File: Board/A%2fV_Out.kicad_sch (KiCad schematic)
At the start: 12 parts, among them J1 HDMI_A

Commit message: work on hdmi
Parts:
- removed SCL1, SDA1, SH1: Conn_01x01_Pin, Connector_PinHeader_1.00mm:PinHeader_1x01_P1.00mm_Vertical, symbol Connector:Conn_01x01_Pin
- added C23, C33: 47u, Capacitor_SMD:C_0805_2012Metric_Pad1.18x1.45mm_HandSolder, symbol Device:C_Polarized
- added C50, C51: 0.1u, csa_ultracpu:C0603, symbol csa_ultracpu-eagle-import:C-EUC0603
- added JP16, JP17, JP18: SolderJumper_2_Open, Jumper:SolderJumper-2_P1.3mm_Open_RoundedPad1.0x1.5mm, symbol Jumper:SolderJumper_2_Open
- added R13, R14, R7, R8: 1k, Resistor_SMD:R_0603_1608Metric_Pad0.98x0.95mm_HandSolder, symbol Device:R
- added U3: ~, Package_DFN_QFN:Diodes_ZL32_TQFN-32-1EP_3x6mm_P0.4mm_EP1.25x3.5mm, symbol HDMI:PI3HDX511Z
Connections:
- net GND: now also J1.SH, C23.2, C33.2, C50.2, C51.2, R14.1, R8.1, U3.14 (GND), U3.31 (GND), U3.32 (GND)
- net HDMI-CK+: now also U3.9 (RCK_N); no longer J1.10 (CK+)
- net HDMI-CK-: now also U3.10 (RCK_P); no longer J1.12 (CK-)
- net HDMI-D0+: now also U3.7 (RD0_N); no longer J1.7 (D0+)
- net HDMI-D0-: now also U3.8 (RD0_P); no longer J1.9 (D0-)
- net HDMI-D1+: now also U3.5 (RD1_N); no longer J1.4 (D1+)
- net HDMI-D1-: now also U3.6 (RD1_P); no longer J1.6 (D1-)
- net HDMI-D2+: now also U3.3 (RD2_N); no longer J1.1 (D2+)
- net HDMI-D2-: now also U3.4 (RD2_P); no longer J1.3 (D2-)
- net at J1.15 (SCL): now also U3.27 (SCL_SINK)
- net at HPD1.1 (Pin_1): now also U3.11 (HPD_SRC); no longer J1.19 (HPD)
- net at J1.16 (SDA): now also U3.28 (SDA_SINK)
- new net: JP17.1 (A), R8.2
- new net: JP17.2 (B), U3.16 (OC_S0)
- new net: R14.2, U3.15 (TEST)
- new net: JP16.1 (A), R13.2
- new net: JP16.2 (B), U3.30 (/OE)
- new net: C23.1, U3.2 (CEXT)
- new net: JP18.2 (B), U3.17 (EQ_S0)
- new net: J1.12 (CK-), U3.18 (TCK_P)
- new net: J1.10 (CK+), U3.19 (TCK_N)
- new net: J1.9 (D0-), U3.20 (TD0_P)
- new net: J1.7 (D0+), U3.21 (TD0_N)
- new net: J1.6 (D1-), U3.23 (TD1_P)
- new net: J1.4 (D1+), U3.24 (TD1_N)
- new net: J1.3 (D2-), U3.25 (TD2_P)
- new net: J1.1 (D2+), U3.26 (TD2_N)
- new net: J1.19 (HPD), U3.29 (HPD_SINK)
- new net: JP18.1 (A), R7.2
- new net I2C_SCL: U3.13 (SCL_SRC)
- new net I2C_SDA: U3.12 (SDA_SRC)
- new net V33: C33.1, C50.1, C51.1, R13.1, R7.1, U3.1 (VCC), U3.22 (VCC)
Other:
- note added: "Note: PI3HDX511D datasheet has reference schematics that also swap signal polarities (on differential signals)"
- note added: "V1.0B: - Added "Brown Fix" V1.1A: - 3.3/5V level converter - VGA ESD protection diodes V1.4A: - go from RGBI to 6bit RGB (2b/col) (replacing IC6 "brownfix" in the process V2.2A: - go from VGA to HDMI - add HDMI re-driver IC"
- note removed: "V1.0B: - Added "Brown Fix" V1.1A: - 3.3/5V level converter - VGA ESD protection diodes V1.4A: - go from RGBI to 6bit RGB (2b/col) (replacing IC6 "brownfix" in the process V2.2A: - go from VGA to HDMI"
- moved on the sheet: CEC1, CKS1, D0S1, D1S1, D2S1, HPD1, J1, JP14, UTIL1

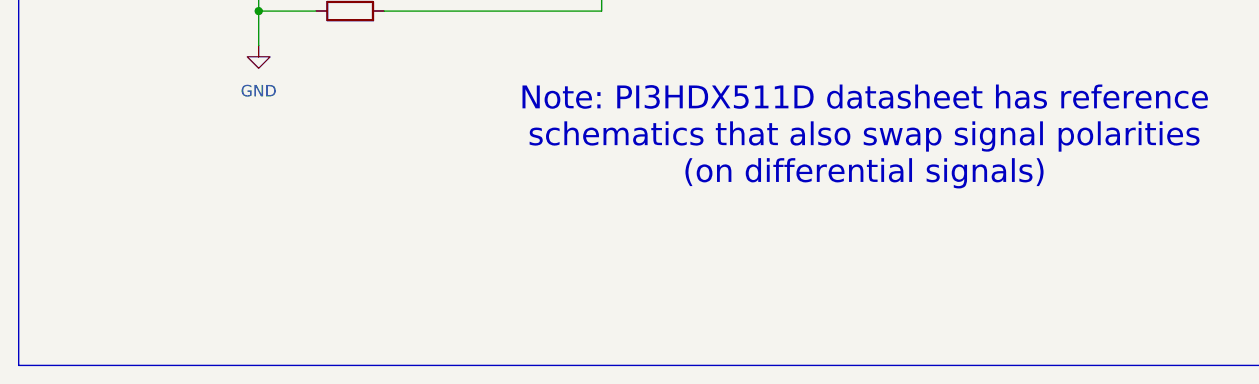
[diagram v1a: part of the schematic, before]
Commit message: start working on 3.0 with larger FPGA
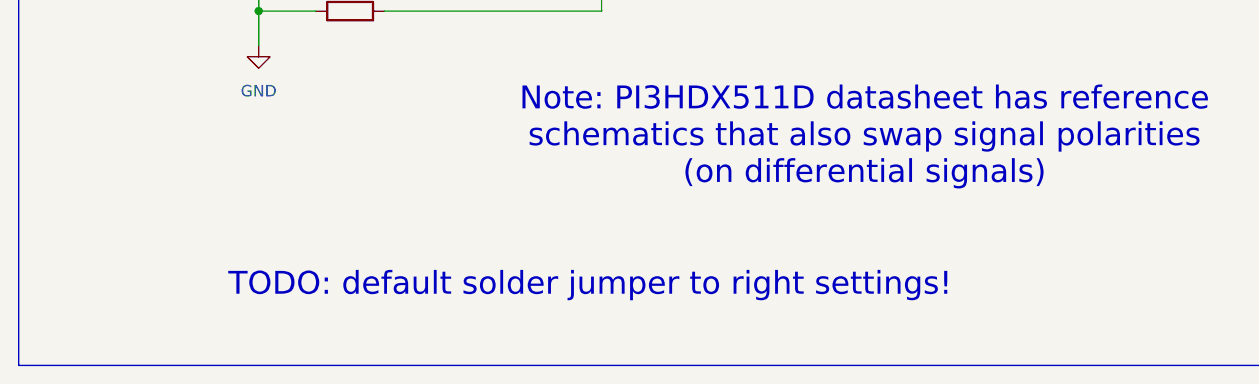
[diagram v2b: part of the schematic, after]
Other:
- note added: "TODO: default solder jumper to right settings!"
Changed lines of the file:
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@@
+		)
+	)
+	(text "TODO: default solder jumper to right settings!\n"
+		(exclude_from_sim no)
+		(at 71.12 166.37 0)
+		(effects
+			(font
+				(size 2.54 2.54)
+			)
 		)
 	)

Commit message: layout work
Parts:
- added C52, C53, C59, C60, C61, C62, C63, C72: 100n, Capacitor_SMD:C_0603_1608Metric_Pad1.08x0.95mm_HandSolder, symbol csa_ultracpu-eagle-import:C-EUC0603
- C50, C51: value 0.1u -> 100n; footprint csa_ultracpu:C0603 -> Capacitor_SMD:C_0603_1608Metric_Pad1.08x0.95mm_HandSolder
- U3: value ~ -> (none)
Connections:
- net HDMI-CK+: now also C62.1; no longer U3.9 (RCK_N)
- net HDMI-CK-: now also C72.1; no longer U3.10 (RCK_P)
- net HDMI-D0+: now also C61.1; no longer U3.7 (RD0_N)
- net HDMI-D0-: now also C63.1; no longer U3.8 (RD0_P)
- net HDMI-D1+: now also C59.1; no longer U3.5 (RD1_N)
- net HDMI-D1-: now also C60.1; no longer U3.6 (RD1_P)
- net HDMI-D2+: now also C52.1; no longer U3.3 (RD2_N)
- net HDMI-D2-: now also C53.1; no longer U3.4 (RD2_P)
- new net: C53.2, U3.4 (RD2_P)
- new net: C61.2, U3.7 (RD0_N)
- new net: C62.2, U3.9 (RCK_N)
- new net: C63.2, U3.8 (RD0_P)
- new net: C72.2, U3.10 (RCK_P)
- new net: C52.2, U3.3 (RD2_N)
- new net: C59.2, U3.5 (RD1_N)
- new net: C60.2, U3.6 (RD1_P)
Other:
- moved on the sheet: C33, C50, C51, HPD1

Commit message: more layout work
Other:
- note added: "CSA-ULTRACPU-V3.0A"
- note removed: "CSA-ULTRACPU-V2.2A"
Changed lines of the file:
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@@
 		)
 	)
-	(text "CSA-ULTRACPU-V2.2A"
+	(text "CSA-ULTRACPU-V3.0A"
 		(exclude_from_sim no)
 		(at 208.28 144.78 0)

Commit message: more layout work
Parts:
- removed CKS1, D0S1, D1S1, D2S1, HPD1: Conn_01x01_Pin, Connector_PinHeader_1.00mm:PinHeader_1x01_P1.00mm_Vertical, symbol Connector:Conn_01x01_Pin
- removed JP14: JP1E, csa_ultracpu:JP1, symbol csa_ultracpu-eagle-import:JP1E
- added JP19: SolderJumper_2_Open, Jumper:SolderJumper-2_P1.3mm_Open_RoundedPad1.0x1.5mm, symbol Jumper:SolderJumper_2_Open
- added JP4: SolderJumper_2_Bridged, Jumper:SolderJumper-2_P1.3mm_Bridged_RoundedPad1.0x1.5mm, symbol Jumper:SolderJumper_2_Bridged
- U3: LCSC C2674166 -> C2674182
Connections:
- net GND: now also J1.11 (CKS), J1.2 (D2S), J1.5 (D1S), J1.8 (D0S)
- net VCC: now also JP4.1 (A)
- net at J1.18 (+5V): now also JP4.2 (B)
- net at R14.2: now also JP19.1 (A); no longer U3.15 (TEST)
- net HPD_SRC: now reaches U3.11 (HPD_SRC)
- new net: JP19.2 (B), U3.15 (ROUT_S0)

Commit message: layout done
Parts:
- C23, C33: LCSC (none) -> C16780
- C50, C51, C52, C53, C59, C60, C61, C62, C63, C72: LCSC (none) -> C14663
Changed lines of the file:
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@@
+			)
+		)
+		(property "LCSC" "C14663"
+			(at 54.61 60.96 0)
+			(hide yes)
+			(show_name no)
+			(do_not_autoplace no)
+			(effects
+				(font
+					(size 1.27 1.27)
+				)
 			)
 		)
@@
 			)
 		)
+		(property "LCSC" "C14663"
+			(at 56.134 41.529 0)
+			(hide yes)
+			(show_name no)
+			(do_not_autoplace no)
+			(effects
+				(font
+					(size 1.27 1.27)
+				)
+			)
+		)
 		(pin "1"
 		)
@@
 		(property "Description" ""
 			(at 40.64 76.2 0)
+			(hide yes)
+			(show_name no)
+			(do_not_autoplace no)
+			(effects
+				(font
+					(size 1.27 1.27)
+				)
+			)
+		)
+		(property "LCSC" "C14663"
+			(at 39.37 73.66 0)
 			(hide yes)
 			(show_name no)
@@
 			)
 		)
+		(property "LCSC" "C14663"
+			(at 47.244 41.529 0)
+			(hide yes)
+			(show_name no)
+			(do_not_autoplace no)
+			(effects
+				(font
+					(size 1.27 1.27)
+				)
+			)
+		)
 		(pin "1"
 		)
@@
 		(property "Description" ""
 			(at 40.64 83.82 0)
+			(hide yes)
+			(show_name no)
+			(do_not_autoplace no)
+			(effects
+				(font
+					(size 1.27 1.27)
+				)
+			)
+		)
+		(property "LCSC" "C14663"
+			(at 39.37 81.28 0)
 			(hide yes)
 			(show_name no)
@@
 			)
 		)
+		(property "LCSC" "C14663"
+			(at 54.61 77.47 0)
+			(hide yes)
+			(show_name no)
+			(do_not_autoplace no)
+			(effects
+				(font
+					(size 1.27 1.27)
+				)
+			)
+		)
 		(pin "1"
 		)
@@
 			)
 		)
+		(property "LCSC" "C14663"
+			(at 54.61 85.09 0)
+			(hide yes)
+			(show_name no)
+			(do_not_autoplace no)
+			(effects
+				(font
+					(size 1.27 1.27)
+				)
+			)
+		)
 		(pin "1"
 		)
@@
 			)
 		)
+		(property "LCSC" "C16780"
+			(at 119.38 115.9509 0)
+			(hide yes)
+			(show_name no)
+			(do_not_autoplace no)
+			(effects
+				(font
+					(size 1.27 1.27)
+				)
+			)
+		)
 		(pin "2"
 		)
@@
 			)
 		)
+		(property "LCSC" "C14663"
+			(at 39.37 57.15 0)
+			(hide yes)
+			(show_name no)
+			(do_not_autoplace no)
+			(effects
+				(font
+					(size 1.27 1.27)
+				)
+			)
+		)
 		(pin "1"
 		)
@@
 		(property "Description" ""
 			(at 46.99 71.12 0)
+			(hide yes)
+			(show_name no)
+			(do_not_autoplace no)
+			(effects
+				(font
+					(size 1.27 1.27)
+				)
+			)
+		)
+		(property "LCSC" "C14663"
+			(at 54.61 68.58 0)
 			(hide yes)
 			(show_name no)
@@
 			)
 		)
+		(property "LCSC" "C14663"
+			(at 39.37 64.77 0)
+			(hide yes)
+			(show_name no)
+			(do_not_autoplace no)
+			(effects
+				(font
+					(size 1.27 1.27)
+				)
+			)
+		)
 		(pin "1"
 		)
@@
 			(hide yes)
 			(show_name no)
+			(do_not_autoplace no)
+			(effects
+				(font
+					(size 1.27 1.27)
+				)
+			)
+		)
+		(property "LCSC" "C16780"
+			(at 67.31 41.0209 0)
+			(hide yes)
+			(show_name no)
